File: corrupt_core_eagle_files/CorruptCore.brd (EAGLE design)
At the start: 100 x 58 mm, 91 parts, among them K1 DTS-3, K10 DTS-3, K11 DTS-3, K12 DTS-3, K13 DTS-3, K14 DTS-3, K15 DTS-3, K16 DTS-3, K2 DTS-3, K3 DTS-3, K4 DTS-3, K5 DTS-3, K6 DTS-3, K7 DTS-3, K8 DTS-3, K9 DTS-3, U1 MEGA8-P, U2 SNX4HC595SOIC16, U3 SNX4HC595SOIC16, U4 SNX4HC595SOIC16, U5 ULN2803ASOIC18, U6 ULN2803ASOIC18, U7 ULN2803ASOIC18, U8 LTC1799, Y1 16MHz

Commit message: apparently I never pushed this
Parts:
- moved T4 3.89 mm to (49.6, 37.1)
- moved T3 3.34 mm to (49.6, 40.4)
- moved T2 2.91 mm to (49.6, 43.5)
- moved T1 2.65 mm to (49.6, 46.8)
- moved 5V@POT1 0.35 mm to (97.8, 30.7)
- moved B1_P1 0.25 mm to (61.5, 53.3)
- moved B1_P2 0.25 mm to (61.5, 50.8)
- moved B1_P3 0.25 mm to (61.5, 48.3)
- moved B1_P4 0.25 mm to (61.5, 45.8)
- moved B1_P5 0.25 mm to (61.5, 43.3)
- moved B1_P6 0.25 mm to (61.5, 40.8)
- moved B1_P7 0.25 mm to (61.5, 38.3)
- moved B1_P8 0.25 mm to (61.5, 35.8)
- moved B2_P1 0.25 mm to (70.0, 53.3)
- moved B2_P2 0.25 mm to (70.0, 50.8)
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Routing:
- net +5V: track 0.00 -> 267.4 mm, vias 0 -> 13
- net POT3: track 0.00 -> 97.8 mm, vias 0 -> 3
- net B2_P1: track 0.00 -> 94.2 mm, vias 0 -> 1
- net B2_P2: track 0.00 -> 92.0 mm, vias 0 -> 1
- net POT2: track 0.00 -> 90.4 mm, vias 0 -> 3
- net POT1: track 0.00 -> 90.3 mm, vias 0 -> 1
- net B1_P6: track 0.00 -> 87.5 mm, vias 0 -> 2
- net B2_P3: track 0.00 -> 87.3 mm, vias 0 -> 1
- net B2_P4: track 0.00 -> 82.8 mm, vias 0 -> 1
- net B1_P5: track 0.00 -> 80.7 mm
- net B1_P7: track 0.00 -> 79.2 mm
- net QP3: track 0.00 -> 78.7 mm, vias 0 -> 3
- net B2_P5: track 0.00 -> 78.2 mm, vias 0 -> 1
- net B3_P1: track 0.00 -> 77.8 mm
- net B3_P2: track 0.00 -> 77.3 mm
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- added copper zone on layer 1, net GND
- added copper zone on layer 16, net GND
- removed copper zone on layer 1, net N$15

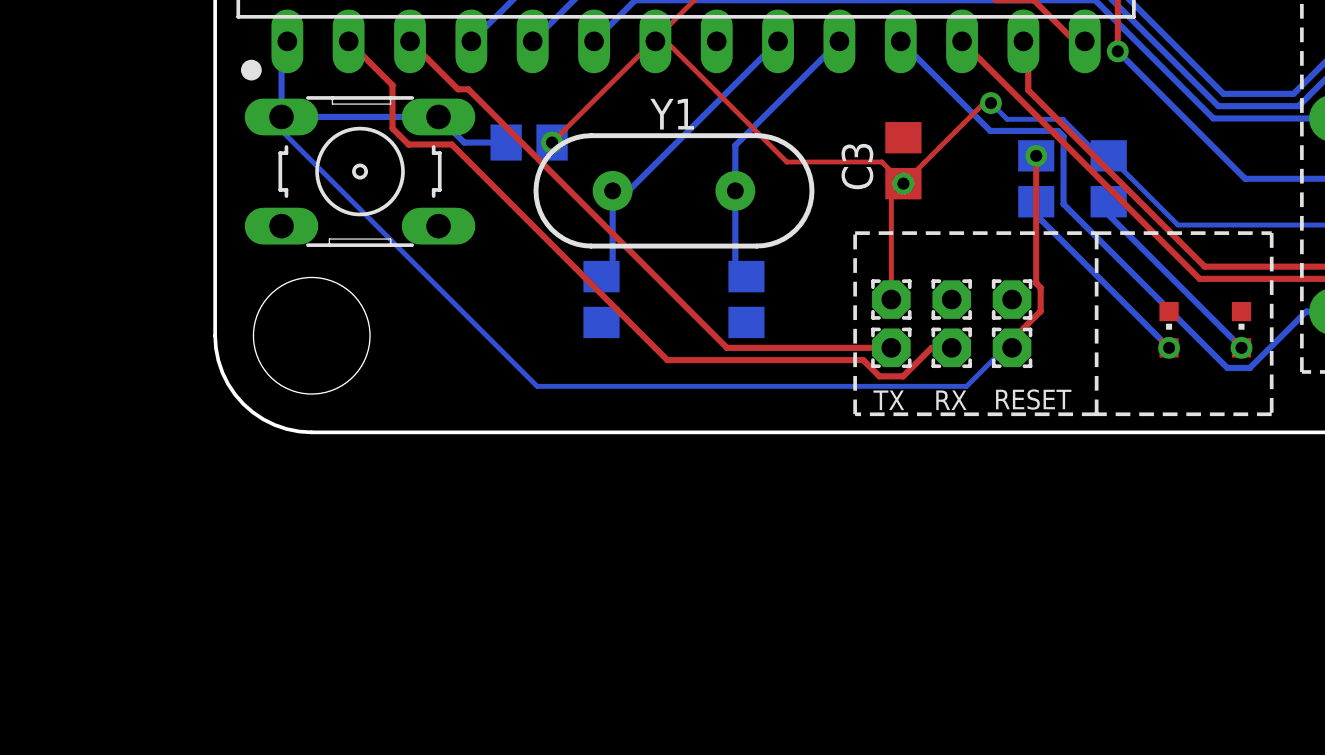
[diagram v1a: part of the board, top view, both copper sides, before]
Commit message: -I was a dummy and wired up the RESET status LED wrong, causing a voltage drop that held the RESET line low no matter what. I fixed it so it just uses a transistor to control the RESET LED.
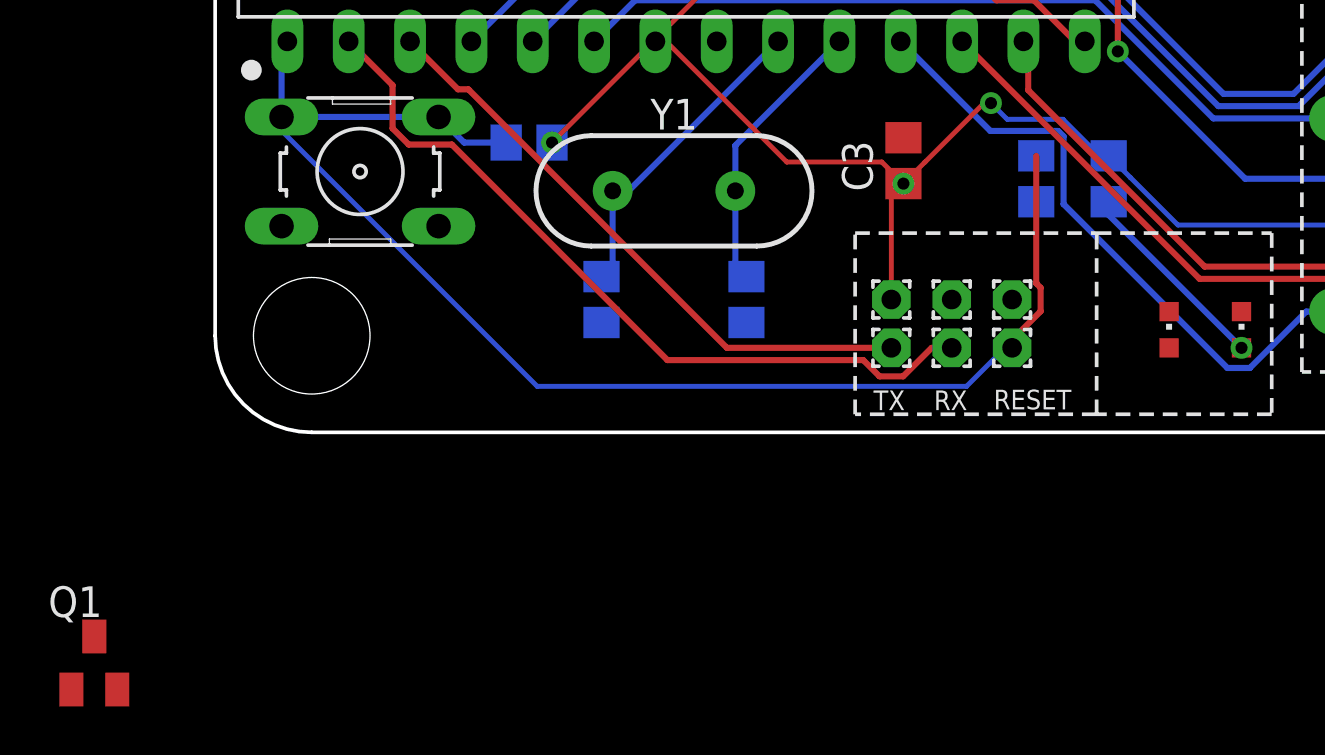
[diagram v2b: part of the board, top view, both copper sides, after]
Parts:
- added Q1: (no value), semicon-smd-ipc:SOT23
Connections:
- new net N$17: Q1.3, RESET_LED.C
- net +5V: now also R2.1
- net GND: now also Q1.2; no longer RESET_LED.C
- net N$6: now also R2.2; no longer R2.1
- net RESET: now also Q1.1; no longer R2.2
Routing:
- net N$6: track 8.33 -> 0.00 mm, vias 1 -> 0
- net RESET: vias 1 -> 0
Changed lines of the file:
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@@
 <attribute name="VALUE" x="33" y="6.1" size="0.0254" layer="27"/>
 </element>
+<element name="Q1" library="semicon-smd-ipc" library_urn="urn:adsk.eagle:library:353" package="SOT23" package3d_urn="urn:adsk.eagle:package:26310/1" value="" x="-5.0038" y="-9.5504"/>
 </elements>
 <signals>
@@
 <wire x1="31.4394" y1="29.15270625" x2="31.4394" y2="29.3526" width="0.2032" layer="1"/>
 <wire x1="31.4394" y1="29.3526" x2="31.0388" y2="29.7532" width="0.2032" layer="1"/>
+<contactref element="R2" pad="1"/>
+<wire x1="36.6213125" y1="11.45" x2="34" y2="9.55" width="0" layer="19" extent="16-16"/>
 </signal>
 <signal name="GND">
@@
 <contactref element="U7" pad="9"/>
 <contactref element="PWR_LED" pad="C"/>
-<contactref element="RESET_LED" pad="C"/>
 <contactref element="C3" pad="2"/>
 <contactref element="C4" pad="2"/>
@@
 <wire x1="30.9626" y1="28.321" x2="32.0294" y2="28.321" width="0.2032" layer="16"/>
 <wire x1="32.0294" y1="28.321" x2="33.4264" y2="26.924" width="0.2032" layer="16"/>
+<contactref element="Q1" pad="2"/>
+<wire x1="89" y1="36.2" x2="88.75" y2="51" width="0" layer="19" extent="1-1"/>
+<wire x1="98" y1="26" x2="89.25" y2="34.1" width="0" layer="19" extent="16-16"/>
+<wire x1="98" y1="17" x2="98" y2="26" width="0" layer="19" extent="1-1"/>
+<wire x1="48.6" y1="36.2" x2="89" y2="36.2" width="0" layer="19" extent="1-1"/>
+<wire x1="48.6" y1="39.4" x2="48.6032" y2="36.2532" width="0" layer="19" extent="1-1"/>
+<wire x1="48.6" y1="42.6" x2="48.683125" y2="39.6922" width="0" layer="19" extent="1-1"/>
+<wire x1="48.6" y1="45.8" x2="48.6" y2="42.6" width="0" layer="19" extent="1-1"/>
+<wire x1="34.925" y1="30.48" x2="48.6" y2="36.2" width="0" layer="19" extent="1-1"/>
+<wire x1="32.0294" y1="28.321" x2="34.6176" y2="30.4" width="0" layer="19" extent="1-16"/>
+<wire x1="16.7894" y1="27.0256" x2="20" y2="28.95" width="0" layer="19" extent="16-16"/>
+<wire x1="18.23" y1="24.2642" x2="16.7894" y2="27.0256" width="0" layer="19" extent="1-1"/>
+<wire x1="12.6746" y1="26.8224" x2="16.7894" y2="27.0256" width="0" layer="19" extent="1-1"/>
+<wire x1="28.5892" y1="35.1028" x2="27.9108" y2="30.4" width="0" layer="19" extent="1-1"/>
+<wire x1="8.635" y1="30.4" x2="12.6746" y2="26.8224" width="0" layer="19" extent="1-1"/>
+<wire x1="3.555" y1="35.6" x2="8.6106" y2="31.0468" width="0" layer="19" extent="1-1"/>
+<wire x1="16.555" y1="35.6" x2="21.45" y2="30.4" width="0" layer="19" extent="1-16"/>
+<wire x1="20.77" y1="16.19" x2="18.23" y2="23.81" width="0" layer="19" extent="1-1"/>
+<wire x1="28.5" y1="12.2" x2="20.77" y2="16.19" width="0" layer="19" extent="1-1"/>
+<wire x1="30.5" y1="5.5" x2="28.5" y2="12.2" width="0" layer="19" extent="1-1"/>
+<wire x1="33" y1="5.5" x2="30.5" y2="5.5" width="0" layer="19" extent="1-1"/>
+<wire x1="22" y1="4.55" x2="30.5" y2="5.5" width="0" layer="19" extent="16-16"/>
+<wire x1="16" y1="4.55" x2="22" y2="4.55" width="0" layer="19" extent="16-16"/>
+<wire x1="9.2512" y1="8.5394" x2="16" y2="4.55" width="0" layer="19" extent="16-16"/>
+<wire x1="2.7488" y1="8.5394" x2="9.2512" y2="8.5394" width="0" layer="19" extent="1-1"/>
+<wire x1="42.5" y1="5" x2="33" y2="5.5" width="0" layer="19" extent="1-1"/>
+<wire x1="29.92" y1="48.9022" x2="29.555" y2="35.6" width="0" layer="19" extent="1-1"/>
+<wire x1="1.92" y1="48.9022" x2="3.555" y2="35.6" width="0" layer="19" extent="1-1"/>
+<wire x1="-4.0538" y1="-10.6504" x2="2.7488" y2="8.5394" width="0" layer="19" extent="1-1"/>
 </signal>
 <signal name="RESET">
@@
 <contactref element="S1" pad="4"/>
 <contactref element="S1" pad="3"/>
-<contactref element="R2" pad="2"/>
 <contactref element="RESET" pad="1"/>
 <wire x1="12.05" y1="12" x2="10.3118" y2="12" width="0.254" layer="16"/>
@@
 <wire x1="34.1811" y1="5.98923125" x2="34" y2="6.17033125" width="0.254" layer="1"/>
 <wire x1="34" y1="6.17033125" x2="34" y2="11.45" width="0.254" layer="1"/>
-<via x="34" y="11.45" extent="1-16" drill="0.5"/>
 <wire x1="31.115" y1="1.905" x2="32.385" y2="3.175" width="0.2032" layer="16"/>
 <wire x1="13.335" y1="1.905" x2="31.115" y2="1.905" width="0.2032" layer="16"/>
@@
 <wire x1="32.385" y1="3.175" x2="33" y2="3.5" width="0.2032" layer="16"/>
 <wire x1="2.54" y1="12.7" x2="2.7488" y2="13.0606" width="0.2032" layer="16"/>
+<contactref element="Q1" pad="1"/>
+<wire x1="13.335" y1="1.905" x2="-5.9538" y2="-10.6504" width="0" layer="19" extent="1-16"/>
 </signal>
 <signal name="N$3">
@@
 <wire x1="60.579" y1="6.563675" x2="60.786675" y2="6.356" width="0.2032" layer="1"/>
 </signal>
-<signal name="N$6">
-<contactref element="R2" pad="1"/>
-<contactref element="RESET_LED" pad="A"/>
-<wire x1="34" y1="9.55" x2="34" y2="9" width="0.254" layer="16"/>
-<wire x1="34" y1="9" x2="39.5" y2="3.5" width="0.254" layer="16"/>
-<via x="39.5" y="3.5" extent="1-16" drill="0.5"/>
-</signal>
 <signal name="N$7">
 <contactref element="R3" pad="1"/>
@@
 <signal name="N$15">
 </signal>
+<signal name="N$6">
+<contactref element="RESET_LED" pad="A"/>
+<contactref element="R2" pad="2"/>
+<wire x1="39.5" y1="3.5" x2="34" y2="11.45" width="0" layer="19" extent="1-16"/>
+</signal>
+<signal name="N$17">
+<contactref element="Q1" pad="3"/>
+<contactref element="RESET_LED" pad="C"/>
+<wire x1="-5.0038" y1="-8.4504" x2="39.5" y2="5" width="0" layer="19" extent="1-1"/>
+</signal>
 </signals>
 <errors>
@@
 with this version.
 </note>
+<note version="8.3" severity="warning">
+Since Version 8.3, EAGLE supports URNs for individual library
+assets (packages, symbols, and devices). The URNs of those assets
+will not be understood (or retained) with this version.
+</note>
+<note version="8.3" severity="warning">
+Since Version 8.3, EAGLE supports the association of 3D packages
+with devices in libraries, schematics, and board files. Those 3D
+packages will not be understood (or retained) with this version.
+</note>
 </compatibility>

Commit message: -added more functions to the Corrupt Core arduino code -I'm the master at vague commit logs
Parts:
- moved Q1 19.1 mm to (9.50, 2.90)
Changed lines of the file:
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@@
 <attribute name="VALUE" x="33" y="6.1" size="0.0254" layer="27"/>
 </element>
-<element name="Q1" library="semicon-smd-ipc" library_urn="urn:adsk.eagle:library:353" package="SOT23" package3d_urn="urn:adsk.eagle:package:26310/1" value="" x="-5.0038" y="-9.5504"/>
+<element name="Q1" library="semicon-smd-ipc" library_urn="urn:adsk.eagle:library:353" package="SOT23" package3d_urn="urn:adsk.eagle:package:26310/1" value="" x="9.4996" y="2.8956"/>
 </elements>
 <signals>
@@
 <wire x1="29.92" y1="48.9022" x2="29.555" y2="35.6" width="0" layer="19" extent="1-1"/>
 <wire x1="1.92" y1="48.9022" x2="3.555" y2="35.6" width="0" layer="19" extent="1-1"/>
-<wire x1="-4.0538" y1="-10.6504" x2="2.7488" y2="8.5394" width="0" layer="19" extent="1-1"/>
+<wire x1="10.4496" y1="1.7956" x2="2.7488" y2="8.5394" width="0" layer="19" extent="1-1"/>
 </signal>
 <signal name="RESET">
@@
 <wire x1="2.54" y1="12.7" x2="2.7488" y2="13.0606" width="0.2032" layer="16"/>
 <contactref element="Q1" pad="1"/>
-<wire x1="13.335" y1="1.905" x2="-5.9538" y2="-10.6504" width="0" layer="19" extent="1-16"/>
+<wire x1="13.335" y1="1.905" x2="8.5496" y2="1.7956" width="0" layer="19" extent="1-16"/>
 </signal>
 <signal name="N$3">
@@
 <contactref element="Q1" pad="3"/>
 <contactref element="RESET_LED" pad="C"/>
-<wire x1="-5.0038" y1="-8.4504" x2="39.5" y2="5" width="0" layer="19" extent="1-1"/>
+<wire x1="9.4996" y1="3.9956" x2="39.5" y2="5" width="0" layer="19" extent="1-1"/>
 </signal>
 </signals>
